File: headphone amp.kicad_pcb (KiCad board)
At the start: 2 copper layers, 100 x 100 mm, 48 parts, among them J1 USB_B_Micro, J2 AudioJack2_Ground_Switch, J3 AudioJack2_Ground_Switch, U1 MAX660CPA+, U2 MAX660CPA+, U3 NE5532, U4 NE5532, U5 NE5532, U6 NE5532

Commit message: Edge Cuts fix
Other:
- board size 100 x 100 mm -> 99.9 x 99.9 mm
- board text added: "2022"
- board text added: "HK Productions"

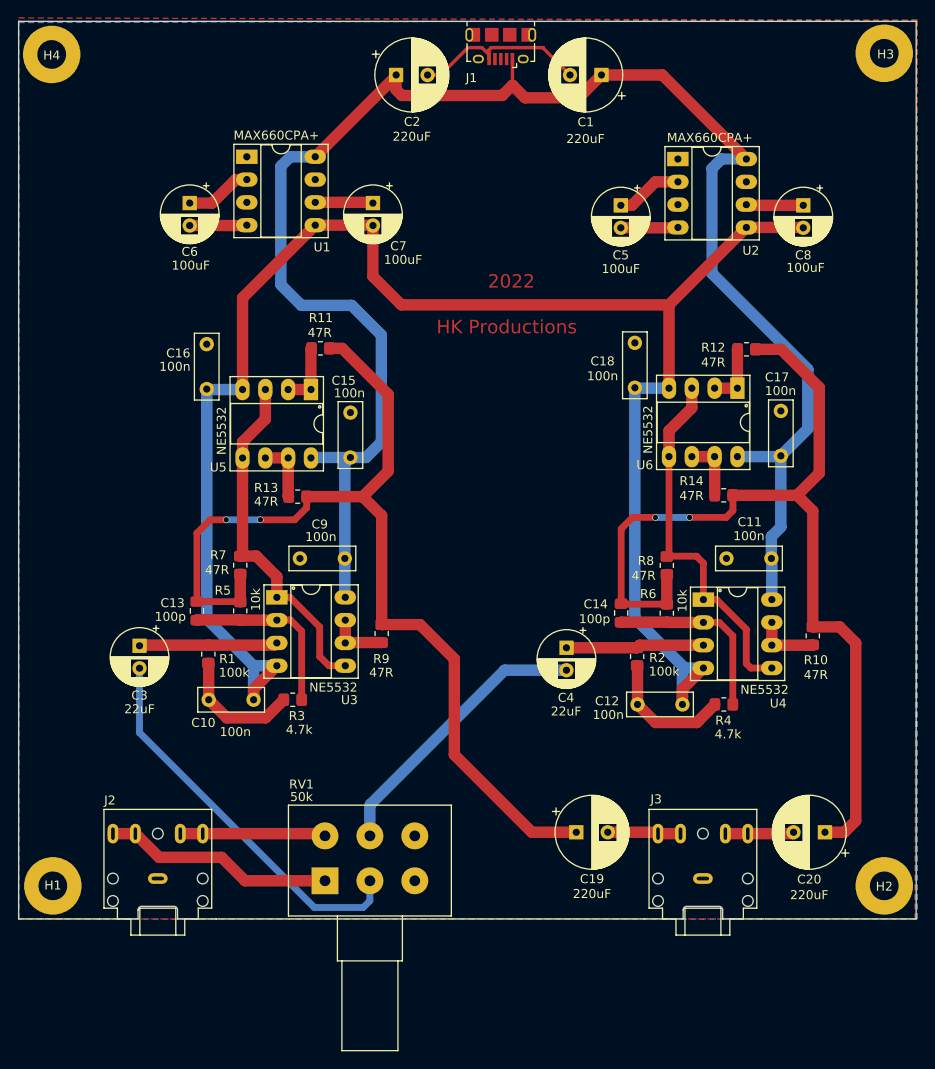
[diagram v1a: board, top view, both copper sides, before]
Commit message: Rounded Corners, Signature and Updated Fab files
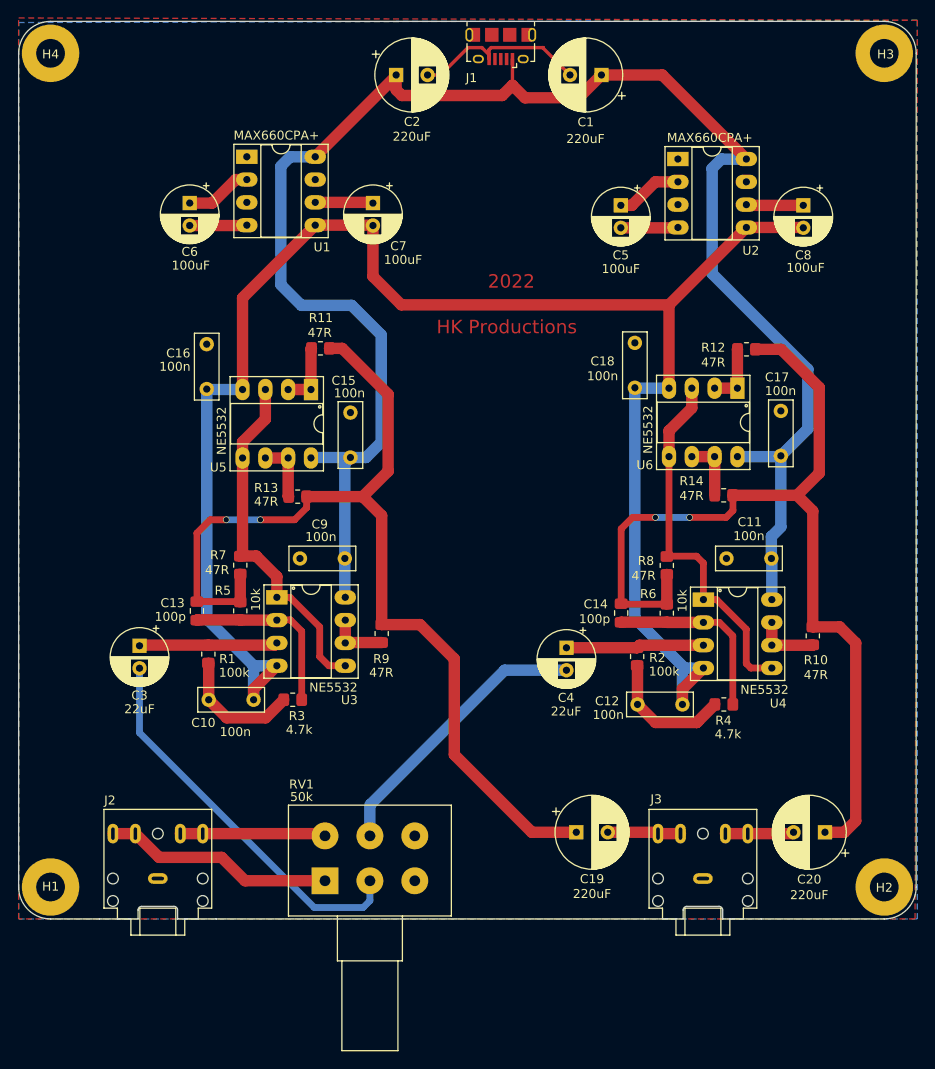
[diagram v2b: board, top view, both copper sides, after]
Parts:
- moved H1 0.28 mm to (103.6, 146.4)
- moved H4 0.18 mm to (103.6, 53.6)
- moved H2 0.13 mm to (196.4, 146.4)
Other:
- outline, holes or cut-outs redrawn
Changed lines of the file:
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@@
       (drillshape 0)
       (scaleselection 1)
-      (outputdirectory "C:/Users/Kori/Desktop/gyarto/")
+      (outputdirectory "C:/Users/Kori/Desktop/Random/Egyetem/2022-2023-1/modul/headphone amp/headphone amp/gyarto/")
     )
   )
@@
   )
   (footprint "MountingHole:MountingHole_3.2mm_M3_Pad" (layer "F.Cu")
-    (at 103.683 53.734)
+    (at 103.556 53.607)
     (descr "Mounting Hole 3.2mm, M3")
     (tags "mounting hole 3.2mm m3")
@@
       (effects (font (size 1 1) (thickness 0.15)))
     )
-    (fp_text value "MountingHole_Pad" (at -3.282 -4.465) (layer "F.Fab")
+    (fp_text value "MountingHole_Pad" (at -3.175 -4.445) (layer "F.Fab")
       (effects (font (size 1 1) (thickness 0.15)))
     )
@@
   )
   (footprint "MountingHole:MountingHole_3.2mm_M3_Pad" (layer "F.Cu")
-    (at 196.393 146.317)
+    (at 196.393 146.444)
     (descr "Mounting Hole 3.2mm, M3")
     (tags "mounting hole 3.2mm m3")
@@
   )
   (footprint "MountingHole:MountingHole_3.2mm_M3_Pad" (layer "F.Cu")
-    (at 103.81 146.317)
+    (at 103.556 146.444)
     (descr "Mounting Hole 3.2mm, M3")
     (tags "mounting hole 3.2mm m3")
@@
   (gr_circle (center 130.607 113.167366) (end 130.48 113.141366) (layer "F.SilkS") (width 0.15) (fill none))
   (gr_circle (center 181.026 92.847366) (end 180.899 92.821366) (layer "F.SilkS") (width 0.15) (fill none))
-  (gr_line (start 199.949 150) (end 182.7 150) (layer "Edge.Cuts") (width 0.1))
-  (gr_line (start 109 150) (end 100 150) (layer "Edge.Cuts") (width 0.1))
-  (gr_line (start 199.949 50.051) (end 199.949 150) (layer "Edge.Cuts") (width 0.15))
-  (gr_line (start 100 50.051) (end 199.949 50.051) (layer "Edge.Cuts") (width 0.15))
-  (gr_line (start 100 150) (end 100 50.051) (layer "Edge.Cuts") (width 0.15))
+  (gr_line (start 109 150) (end 103.556 150) (layer "Edge.Cuts") (width 0.1))
+  (gr_arc (start 199.949 146.444) (mid 198.907472 148.958472) (end 196.393 150) (layer "Edge.Cuts") (width 0.1))
+  (gr_line (start 100 146.444) (end 100 53.607) (layer "Edge.Cuts") (width 0.1))
+  (gr_arc (start 196.393 50.051) (mid 198.907472 51.092528) (end 199.949 53.607) (layer "Edge.Cuts") (width 0.1))
+  (gr_line (start 199.949 53.607) (end 199.949 146.444) (layer "Edge.Cuts") (width 0.1))
+  (gr_arc (start 103.556 150) (mid 101.041528 148.958472) (end 100 146.444) (layer "Edge.Cuts") (width 0.1))
+  (gr_arc (start 100 53.607) (mid 101.041528 51.092528) (end 103.556 50.051) (layer "Edge.Cuts") (width 0.1))
+  (gr_line (start 196.393 150) (end 182.7 150) (layer "Edge.Cuts") (width 0.1))
+  (gr_line (start 103.556 50.051) (end 196.393 50.051) (layer "Edge.Cuts") (width 0.1))
   (gr_line (start 169.7 150) (end 122 150) (layer "Edge.Cuts") (width 0.1))
   (gr_text "2022\n" (at 154.864 79.007) (layer "F.Cu")

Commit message: Fixed one wire and added silly graphics
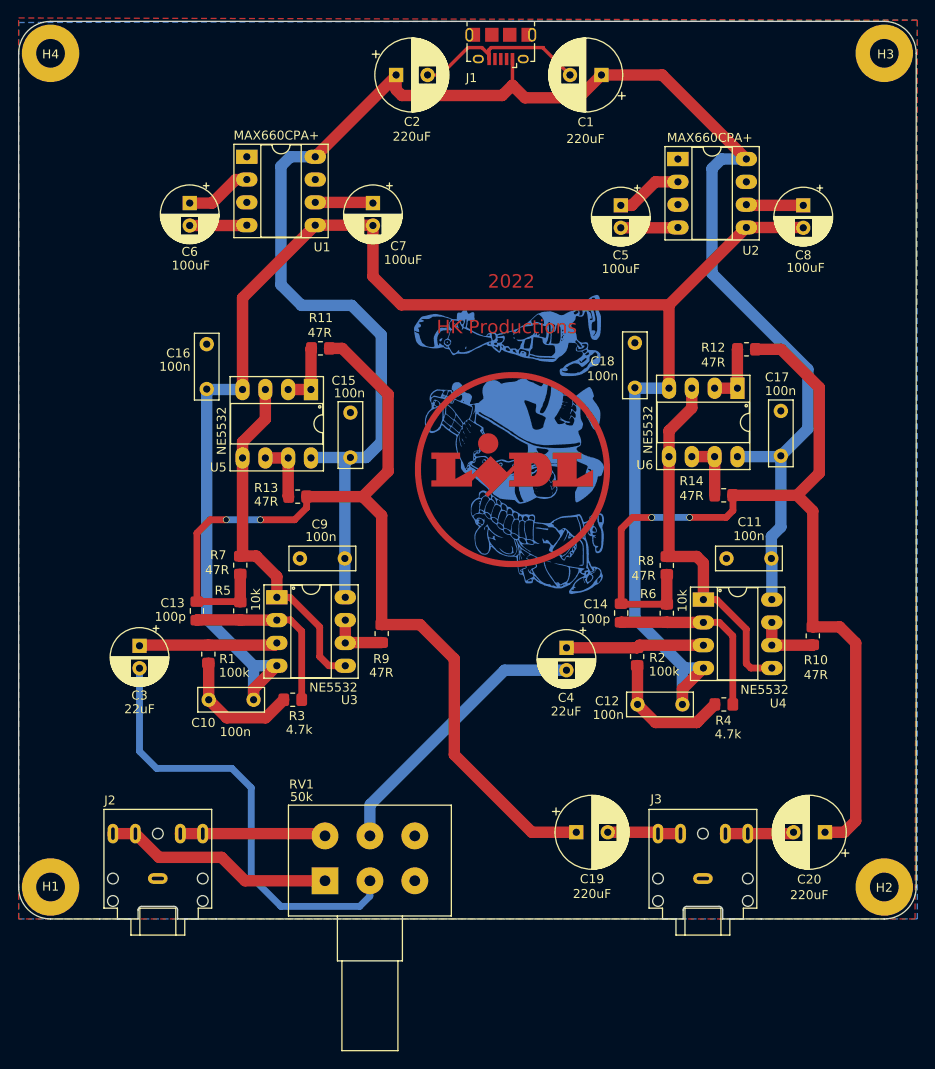
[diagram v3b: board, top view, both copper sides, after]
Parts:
- added G***: LOGO, LOGO, F.Cu at (155.0, 100.0)
- added G***: LOGO, LOGO, B.Cu at (154.3, 97.1)
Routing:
- net Net-(C3-Pad2): track 43.4 -> 50.0 mm

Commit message: Add files via upload
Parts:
- removed G*** (x2): LOGO, LOGO
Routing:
- net GND: track 64.8 -> 67.1 mm
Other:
- board text added: "Hugyik Kornél"
- board text removed: "HK Productions"
